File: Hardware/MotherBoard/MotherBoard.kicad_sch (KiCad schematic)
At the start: 24 parts, among them J1 POWER, J10 I/O_PWR, J13 USB_OTG, J2 I/O0, J5 I/O1, J6 EXTRN_CLCK, J9 Conn_02x02_Odd_Even, SW1 RESET_SW, SW2 ON_OFF, U1 AMS1117-5.0, X1 ACO-1MHz

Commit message: Fix
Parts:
- added F2: 500mA, Resistor_THT:R_Box_L8.4mm_W2.5mm_P5.08mm, symbol Device:Fuse_Small
- U1: footprint Package_TO_SOT_SMD:SOT-223-3_TabPin2 -> Package_TO_SOT_THT:TO-220-3_Horizontal_TabDown
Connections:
- net +5V: now also SW2.2 (B); no longer C2.1, FB2.2, U1.2 (VO)
- net at J13.1 (VBUS): now also F2.1; no longer FB2.1
- net at SW2.1 (A): now also C2.1, FB2.2, U1.2 (VO); no longer J1.1
- net at F1.1: now also J1.1; no longer SW2.2 (B)
- new net: F2.2, FB2.1
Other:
- sheet North Bridge ports: added DMARW, RW; removed none
- sheet South Bridge ports: added DMARW; removed none
- title: Retro 6502 Mother Board -> Miniish
- moved on the sheet: C1, C2, D1, F1, FB1, FB2, H1, H2, H3, H4, J1, J13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

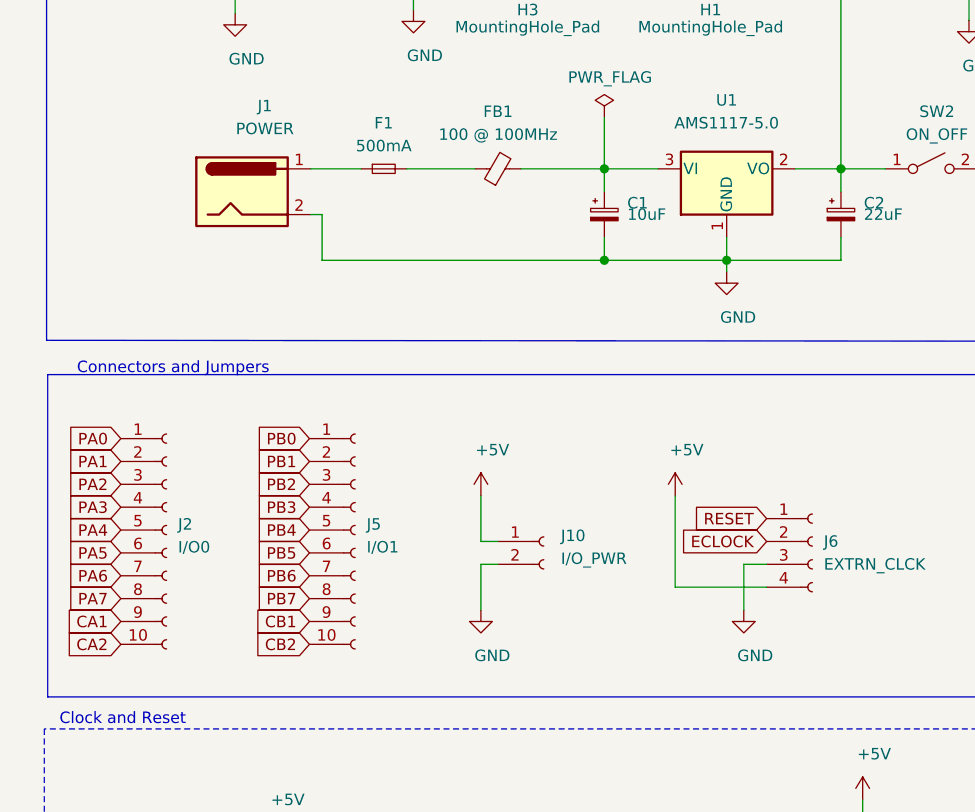
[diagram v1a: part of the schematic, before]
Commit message: Update to Kicad 6.0
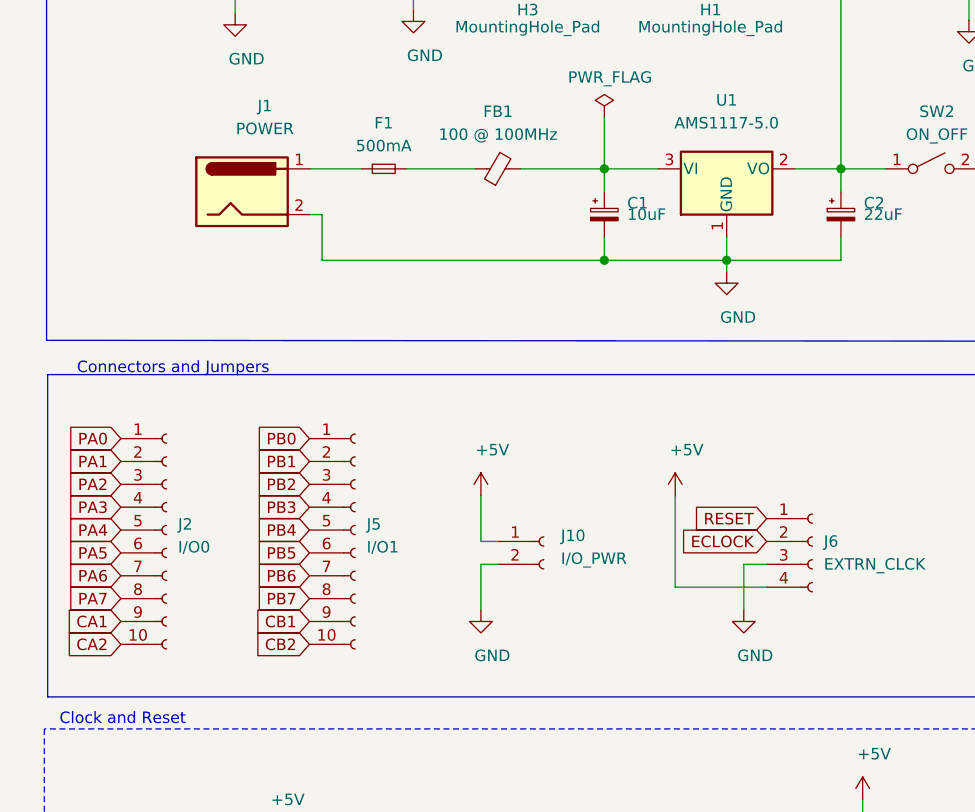
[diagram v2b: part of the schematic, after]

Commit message: New motherboard version
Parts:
- removed C8: 470nF, Capacitor_THT:C_Disc_D5.0mm_W2.5mm_P5.00mm, symbol Device:C_Small
- removed J10: I/O_PWR, Connector_PinSocket_2.54mm:PinSocket_1x02_P2.54mm_Vertical, symbol Connector:Conn_01x02_Female
- removed J2: I/O0, Connector_PinSocket_2.54mm:PinSocket_1x10_P2.54mm_Vertical, symbol Connector:Conn_01x10_Female
- removed J5: I/O1, Connector_PinSocket_2.54mm:PinSocket_1x10_P2.54mm_Vertical, symbol Connector:Conn_01x10_Female
- removed R3: 10K, Resistor_THT:R_Axial_DIN0207_L6.3mm_D2.5mm_P10.16mm_Horizontal, symbol Device:R_Small
- removed SW1: RESET_SW, Button_Switch_THT:SW_Tactile_SPST_Angled_PTS645Vx83-2LFS, symbol Switch:SW_Push
- added C1: 10nF, Capacitor_THT:C_Disc_D5.0mm_W2.5mm_P2.50mm, symbol Device:C
- added J11: CLOCK_DIV, Button_Switch_THT:SW_DIP_SPSTx05_Slide_6.7x14.26mm_W7.62mm_P2.54mm_LowProfile, symbol Switch:SW_DIP_x05
- added U1: 74HC590A, Package_DIP:DIP-16_W7.62mm, symbol 74xx:74HC590A
- C2: renamed from C1; symbol Device:CP_Small -> Device:C_Polarized_Small
- C3: renamed from C2; symbol Device:CP_Small -> Device:C_Polarized_Small
- FB1: renamed from FB2; symbol Device:Ferrite_Bead_Small -> Device:FerriteBead_Small
- FB2: renamed from FB1; symbol Device:Ferrite_Bead_Small -> Device:FerriteBead_Small
- J3: renamed from J9; value Conn_02x02_Odd_Even -> CLOCK_SEL
- J4: renamed from J6; symbol Connector:Conn_01x04_Female -> Connector:Conn_01x04_Socket
- U2: renamed from U1; symbol Regulator_Linear:AMS1117-5.0 -> Regulator_Linear:AZ1117-5.0
- X1: value ACO-1MHz -> ACO-16MHz
- renumbered F2 to F1, F1 to F2, H4 to H1, H3 to H2, H2 to H3, H1 to H4, J13 to J1, J1 to J2, R4 to R1
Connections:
- net +5V: now also C1.1, U1.10 (~{MRC}), U1.16 (VCC)
- net GND: now also C1.2, U1.12 (~{CE}), U1.14 (~{OE}), U1.8 (GND)
- net at J3.1 (Pin_1): now also J11.10, J11.6, J11.7, J11.8, J11.9; no longer X1.8 (OUT)
- new net 16MHz: J11.1, U1.11 (CPC), U1.13 (CPR), X1.8 (OUT)
- new net 1MHz: J11.5, U1.3 (Q3)
- new net 2MHz: J11.4, U1.2 (Q2)
- new net 4MHz: J11.3, U1.1 (Q1)
- new net 8MHz: J11.2, U1.15 (Q0)
- no-connect marks 3 -> 8
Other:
- removed sheet Main 
- added sheet GPIO (gpio.kicad_sch)
- added sheet Ports (ports.kicad_sch)
- sheet North Bridge: file /home/romuald/Projects/Miniish/Hardware/MotherBoard/NorthBridge.kicad_sch -> NorthBridge.kicad_sch
- sheet North Bridge ports: added NMIB, RESET; removed DMARW, IOCSB, IRQ0B, IRQ1B, PORT1B, PORT2B, ROMCSB
- sheet South Bridge: file /home/romuald/Projects/Miniish/Hardware/MotherBoard/SouthBridge.kicad_sch -> SouthBridge.kicad_sch
- sheet South Bridge ports: added CIA1CSB, CIA2CSB, IRQ1B, IRQ2B, IRQ3B, IRQ4B, IRQ5B, IRQ6B, IRQB, PORT1CSB, PORT2CSB, PORT3CSB, RAMCSB, ROMCSB, USRCSB; removed DMARW, NMIB, PORT1B, PORT2B, RESET, RW
- note added: "Clock"
- note removed: "Clock and Reset"
- note removed: "Connectors and Jumpers"
- moved on the sheet: H1, H2, H3, H4, J2, J3, J4, X1

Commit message: Finalize 1.3
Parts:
- J11: value CLOCK_DIV -> CLOCK_SPD
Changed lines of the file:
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@@
   (title_block
     (title "Miniish")
-    (date "2020-10-10")
+    (date "2023-05-19")
     (rev "v1.3")
     (company "Romuald Rousseau")
@@
       (effects (font (size 1.27 1.27)))
     )
-    (property "Value" "CLOCK_DIV" (at 102.87 95.25 0)
-      (effects (font (size 1.27 1.27)))
-    )
+    (property "Value" "CLOCK_SPD" (at 102.87 95.25 0)
+      (effects (font (size 1.27 1.27)))
+    )

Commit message: Version 1.3
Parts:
- added C1: 100nF, Capacitor_THT:C_Disc_D5.0mm_W2.5mm_P2.50mm, symbol Device:C
- C1: value 10nF -> 100nF
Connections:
- net GND: now also C1.2
- net RESET: now also C1.1
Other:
- moved on the sheet: J4
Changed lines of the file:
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@@
     (stroke (width 0) (type default))
   )
-  (wire (pts (xy 116.84 128.27) (xy 114.3 128.27))
+  (wire (pts (xy 119.38 129.54) (xy 116.84 129.54))
     (stroke (width 0) (type solid))
   )
@@
     (stroke (width 0) (type solid))
   )
-  (wire (pts (xy 114.3 128.27) (xy 114.3 133.35))
+  (wire (pts (xy 99.06 124.46) (xy 99.06 125.73))
+    (stroke (width 0) (type default))
+  )
+  (wire (pts (xy 116.84 129.54) (xy 116.84 134.62))
     (stroke (width 0) (type solid))
   )
@@
     (stroke (width 0) (type default))
   )
+  (wire (pts (xy 99.06 133.35) (xy 99.06 134.62))
+    (stroke (width 0) (type default))
+  )
   (wire (pts (xy 193.04 140.97) (xy 177.8 140.97))
     (stroke (width 0) (type default))
@@
     (stroke (width 0) (type default))
   )
-  (wire (pts (xy 106.68 120.65) (xy 106.68 130.81))
+  (wire (pts (xy 109.22 121.92) (xy 109.22 132.08))
     (stroke (width 0) (type solid))
   )
@@
     (stroke (width 0) (type solid))
   )
-  (wire (pts (xy 106.68 130.81) (xy 116.84 130.81))
+  (wire (pts (xy 109.22 132.08) (xy 119.38 132.08))
     (stroke (width 0) (type solid))
   )
@@
     (stroke (width 0) (type dash))
   )
+  (wire (pts (xy 119.38 124.46) (xy 99.06 124.46))
+    (stroke (width 0) (type default))
+  )
   (wire (pts (xy 177.8 104.14) (xy 177.8 55.88))
     (stroke (width 0) (type default))
@@
     (effects (font (size 1.27 1.27)) (justify left bottom))
   )
-  (global_label "ECLOCK" (shape input) (at 116.84 125.73 180)
+  (global_label "ECLOCK" (shape input) (at 119.38 127 180)
     (effects (font (size 1.27 1.27)) (justify right))
-    (property "Intersheetrefs" "${INTERSHEET_REFS}" (at 15.875 20.32 0)
-      (effects (font (size 1.27 1.27)) hide)
-    )
-  )
-  (global_label "RESET" (shape input) (at 116.84 123.19 180)
+    (property "Intersheetrefs" "${INTERSHEET_REFS}" (at 18.415 21.59 0)
+      (effects (font (size 1.27 1.27)) hide)
+    )
+  )
+  (global_label "RESET" (shape input) (at 99.06 124.46 180)
     (effects (font (size 1.27 1.27)) (justify right))
-    (property "Intersheetrefs" "${INTERSHEET_REFS}" (at 15.875 20.32 0)
+    (property "Intersheetrefs" "${INTERSHEET_REFS}" (at -1.905 21.59 0)
       (effects (font (size 1.27 1.27)) hide)
     )
@@
     )
   )
-  (symbol (lib_id "Connector:Conn_01x04_Socket") (at 121.92 125.73 0) (unit 1)
-    (in_bom yes) (on_board yes) (dnp no)
-    (property "Reference" "J4" (at 123.19 125.73 0)
+  (symbol (lib_id "Connector:Conn_01x04_Socket") (at 124.46 127 0) (unit 1)
+    (in_bom yes) (on_board yes) (dnp no)
+    (property "Reference" "J4" (at 125.73 127 0)
       (effects (font (size 1.27 1.27)) (justify left))
     )
-    (property "Value" "EXTRN_CLCK" (at 123.19 128.27 0)
+    (property "Value" "EXTRN_CLCK" (at 125.73 129.54 0)
       (effects (font (size 1.27 1.27)) (justify left))
     )
-    (property "Footprint" "Connector_PinHeader_2.54mm:PinHeader_1x04_P2.54mm_Vertical" (at 121.92 125.73 0)
-      (effects (font (size 1.27 1.27)) hide)
-    )
-    (property "Datasheet" "~" (at 121.92 125.73 0)
+    (property "Footprint" "Connector_PinHeader_2.54mm:PinHeader_1x04_P2.54mm_Vertical" (at 124.46 127 0)
+      (effects (font (size 1.27 1.27)) hide)
+    )
+    (property "Datasheet" "~" (at 124.46 127 0)
       (effects (font (size 1.27 1.27)) hide)
     )
@@
     )
   )
+  (symbol (lib_id "Device:C") (at 99.06 129.54 0) (unit 1)
+    (in_bom yes) (on_board yes) (dnp no)
+    (property "Reference" "C1" (at 102.108 127.254 0)
+      (effects (font (size 1.27 1.27)) (justify left))
+    )
+    (property "Value" "100nF" (at 102.108 129.794 0)
+      (effects (font (size 1.27 1.27)) (justify left))
+    )
+    (property "Footprint" "Capacitor_THT:C_Disc_D5.0mm_W2.5mm_P2.50mm" (at 100.0252 133.35 0)
+      (effects (font (size 1.27 1.27)) hide)
+    )
+    (property "Datasheet" "~" (at 99.06 129.54 0)
+      (effects (font (size 1.27 1.27)) hide)
+    )
+    (pin "1")
+    (pin "2")
+    (instances
+      (project "DaughterDevBoard"
+        (path "/635897ee-ca46-4488-aee3-87929b6a86bf"
+          (reference "C1") (unit 1)
+        )
+      )
+      (project "MotherBoard"
+        (path "/e63e39d7-6ac0-4ffd-8aa3-1841a4541b55"
+          (reference "C13") (unit 1)
+        )
+      )
+    )
+  )
   (symbol (lib_id "Device:C") (at 24.13 127 0) (unit 1)
     (in_bom yes) (on_board yes) (dnp no)
@@
       (effects (font (size 1.27 1.27)) (justify left))
     )
-    (property "Value" "10nF" (at 27.178 127.254 0)
+    (property "Value" "100nF" (at 27.178 127.254 0)
       (effects (font (size 1.27 1.27)) (justify left))
     )
@@
     )
   )
-  (symbol (lib_id "power:+5V") (at 106.68 120.65 0) (unit 1)
-    (in_bom yes) (on_board yes) (dnp no)
-    (property "Reference" "#PWR010" (at 106.68 124.46 0)
-      (effects (font (size 1.27 1.27)) hide)
-    )
-    (property "Value" "+5V" (at 107.95 115.57 0)
-      (effects (font (size 1.27 1.27)))
-    )
-    (property "Footprint" "" (at 106.68 120.65 0)
-      (effects (font (size 1.27 1.27)) hide)
-    )
-    (property "Datasheet" "" (at 106.68 120.65 0)
+  (symbol (lib_id "power:+5V") (at 109.22 121.92 0) (unit 1)
+    (in_bom yes) (on_board yes) (dnp no)
+    (property "Reference" "#PWR010" (at 109.22 125.73 0)
+      (effects (font (size 1.27 1.27)) hide)
+    )
+    (property "Value" "+5V" (at 110.49 116.84 0)
+      (effects (font (size 1.27 1.27)))
+    )
+    (property "Footprint" "" (at 109.22 121.92 0)
+      (effects (font (size 1.27 1.27)) hide)
+    )
+    (property "Datasheet" "" (at 109.22 121.92 0)
       (effects (font (size 1.27 1.27)) hide)
     )
@@
     )
   )
+  (symbol (lib_id "power:GND") (at 99.06 134.62 0) (unit 1)
+    (in_bom yes) (on_board yes) (dnp no)
+    (property "Reference" "#PWR0116" (at 99.06 140.97 0)
+      (effects (font (size 1.27 1.27)) hide)
+    )
+    (property "Value" "GND" (at 100.33 139.7 0)
+      (effects (font (size 1.27 1.27)))
+    )
+    (property "Footprint" "" (at 99.06 134.62 0)
+      (effects (font (size 1.27 1.27)) hide)
+    )
+    (property "Datasheet" "" (at 99.06 134.62 0)
+      (effects (font (size 1.27 1.27)) hide)
+    )
+    (pin "1")
+    (instances
+      (project "DaughterDevBoard"
+        (path "/635897ee-ca46-4488-aee3-87929b6a86bf"
+          (reference "#PWR0116") (unit 1)
+        )
+      )
+      (project "MotherBoard"
+        (path "/e63e39d7-6ac0-4ffd-8aa3-1841a4541b55"
+          (reference "#PWR026") (unit 1)
+        )
+      )
+    )
+  )
   (symbol (lib_id "Mechanical:MountingHole_Pad") (at 90.17 39.37 0) (unit 1)
     (in_bom yes) (on_board yes) (dnp no)
@@
     )
   )
-  (symbol (lib_id "power:GND") (at 114.3 133.35 0) (unit 1)
-    (in_bom yes) (on_board yes) (dnp no)
-    (property "Reference" "#PWR011" (at 114.3 139.7 0)
-      (effects (font (size 1.27 1.27)) hide)
-    )
-    (property "Value" "GND" (at 115.57 138.43 0)
-      (effects (font (size 1.27 1.27)))
-    )
-    (property "Footprint" "" (at 114.3 133.35 0)
-      (effects (font (size 1.27 1.27)) hide)
-    )
-    (property "Datasheet" "" (at 114.3 133.35 0)
-      (effects (font (size 1.27 1.27)) hide)
-    )
+  (symbol (lib_id "power:GND") (at 116.84 134.62 0) (unit 1)
+    (in_bom yes) (on_board yes) (dnp no)
+    (property "Reference" "#PWR011" (at 116.84 140.97 0)
+      (effects (font (size 1.27 1.27)) hide)
+    )
+    (property "Value" "GND" (at 118.11 139.7 0)
+      (effects (font (size 1.27 1.27)))
+    )
+    (property "Footprint" "" (at 116.84 134.62 0)
+      (effects (font (size 1.27 1.27)) hide)
+    )
+    (property "Datasheet" "" (at 116.84 134.62 0)
+      (effects (font (size 1.27 1.27)) hide)
+    )

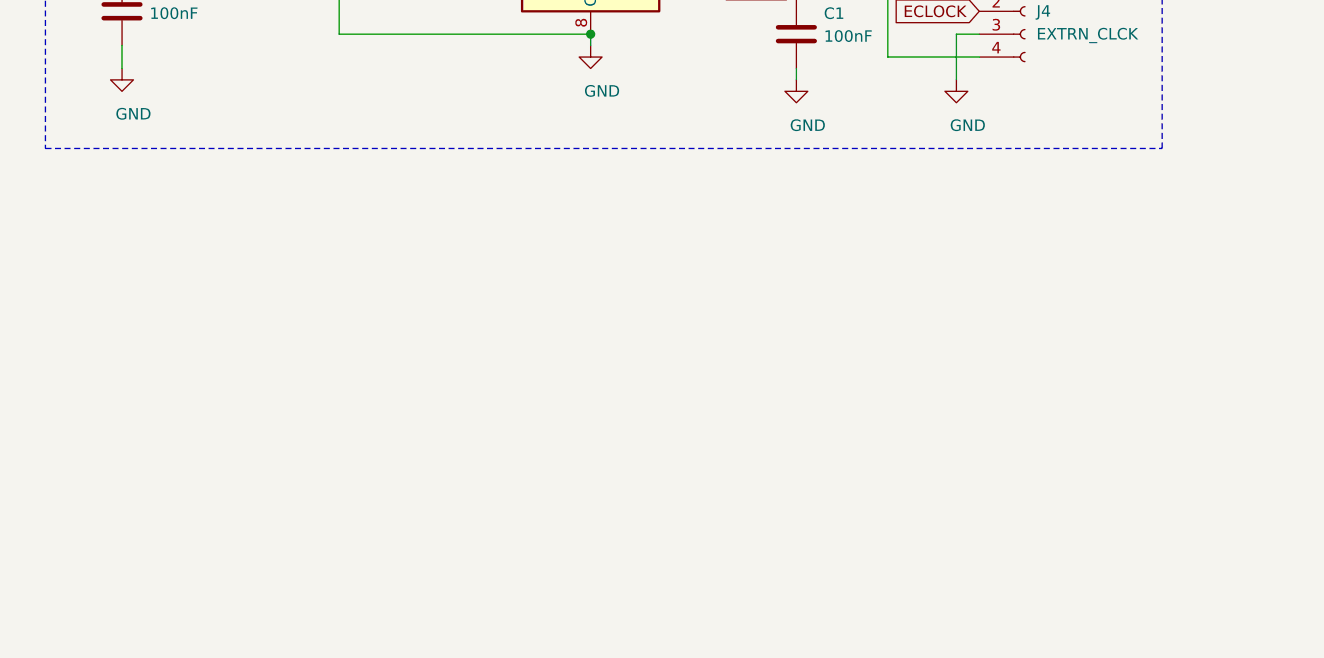
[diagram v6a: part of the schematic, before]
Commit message: Add SPI Board
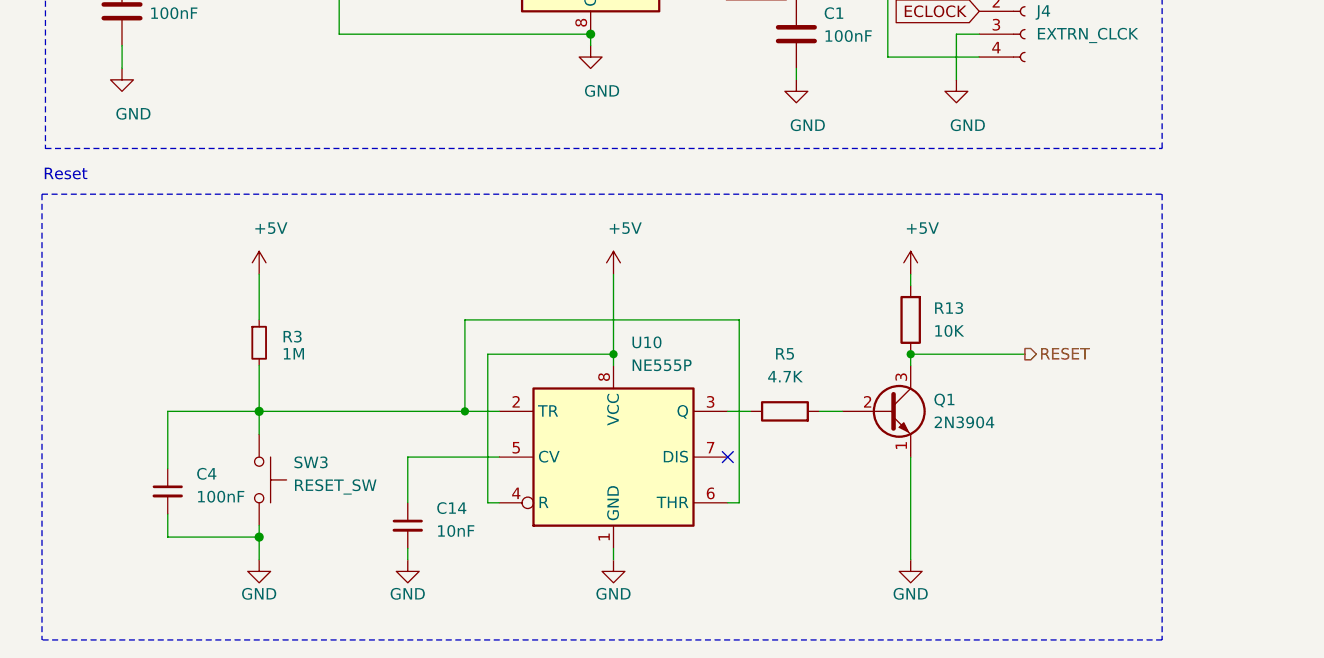
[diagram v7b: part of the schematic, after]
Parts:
- added C14: 10nF, Capacitor_THT:C_Disc_D5.0mm_W2.5mm_P5.00mm, symbol Device:C_Small
- added C4: 100nF, Capacitor_THT:C_Disc_D5.0mm_W2.5mm_P5.00mm, symbol Device:C_Small
- added Q1: 2N3904, Package_TO_SOT_THT:TO-92_Inline, symbol Transistor_BJT:2N3904
- added R13: 10K, Resistor_THT:R_Axial_DIN0207_L6.3mm_D2.5mm_P10.16mm_Horizontal, symbol Device:R
- added R3: 1M, Resistor_THT:R_Axial_DIN0207_L6.3mm_D2.5mm_P10.16mm_Horizontal, symbol Device:R_Small
- added R5: 4.7K, Resistor_THT:R_Axial_DIN0207_L6.3mm_D2.5mm_P10.16mm_Horizontal, symbol Device:R
- added SW3: RESET_SW, Button_Switch_THT:SW_Tactile_SPST_Angled_PTS645Vx83-2LFS, symbol Switch:SW_Push
- added U10: NE555P, Package_DIP:DIP-8_W7.62mm, symbol Timer:NE555P
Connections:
- net +5V: now also R13.2, R3.1, U10.4 (R), U10.8 (VCC)
- net GND: now also C14.2, C4.2, Q1.1 (E), SW3.2, U10.1 (GND)
- net RESET: now also Q1.3 (C), R13.1
- new net: C4.1, R3.2, SW3.1, U10.2 (TR), U10.6 (THR)
- new net: R5.1, U10.3 (Q)
- new net: Q1.2 (B), R5.2
- new net: C14.1, U10.5 (CV)
- no-connect marks 8 -> 9
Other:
- note added: "Reset"

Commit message: A lot of new hardware
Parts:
- removed C2: 10uF, Capacitor_THT:C_Radial_D5.0mm_H11.0mm_P2.00mm, symbol Device:C_Polarized_Small
- removed C3: 22uF, Capacitor_THT:C_Radial_D5.0mm_H11.0mm_P2.00mm, symbol Device:C_Polarized_Small
- removed D1: LED, LED_THT:LED_D5.0mm, symbol Device:LED
- removed F1, F2: 500mA, Resistor_THT:R_Box_L8.4mm_W2.5mm_P5.08mm, symbol Device:Fuse_Small
- removed FB1, FB2: 100 @ 100MHz, Inductor_THT:L_Axial_L9.5mm_D4.0mm_P12.70mm_Horizontal_Fastron_SMCC, symbol Device:FerriteBead_Small
- removed H1, H2, H3, H4: MountingHole_Pad, MountingHole:MountingHole_3.2mm_M3, symbol Mechanical:MountingHole_Pad
- removed J1: USB_OTG, Connector_USB:USB_B_OST_USB-B1HSxx_Horizontal, symbol Connector:USB_B
- removed J2: POWER, Connector_BarrelJack:BarrelJack_Horizontal, symbol Connector:Jack-DC
- removed R1: 220, Resistor_THT:R_Axial_DIN0207_L6.3mm_D2.5mm_P10.16mm_Horizontal, symbol Device:R
- removed U2: AMS1117-5.0, Package_TO_SOT_THT:TO-220-3_Horizontal_TabDown, symbol Regulator_Linear:AZ1117-5.0
- added D3: LED, LED_THT:LED_D5.0mm, symbol Device:LED
- added J25: ATX-24, Connector_Molex:Molex_Mini-Fit_Jr_5566-24A_2x12_P4.20mm_Vertical, symbol Connector:ATX-24
- added R14: 220, Resistor_THT:R_Axial_DIN0207_L6.3mm_D2.5mm_P10.16mm_Horizontal, symbol Device:R
- C14, C4: footprint Capacitor_THT:C_Disc_D5.0mm_W2.5mm_P5.00mm -> Capacitor_THT:C_Disc_D5.0mm_W2.5mm_P2.50mm
- SW3: value RESET_SW -> RESET
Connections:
- net +5V: now also J25.21 (+5V), J25.22 (+5V), J25.23 (+5V), J25.4 (+5V), J25.6 (+5V); no longer R3.1, SW2.2 (B)
- net GND: now also SW2.1 (A), J25.15 (GND), J25.17 (GND), J25.18 (GND), J25.19 (GND), J25.24 (GND), J25.3 (GND), J25.5 (GND), J25.7 (GND), R14.2
- new net: J25.1 (+3.3V), J25.12 (+3.3V), J25.13 (+3.3V), J25.2 (+3.3V)
- new net: J25.10 (+12V), J25.11 (+12V)
- new net: J25.16 (PS_ON#), SW2.2 (B)
- new net: D3.1 (K), R14.1
- new net PWR_OK: D3.2 (A), J25.8 (PWR_OK), R3.1
- no-connect marks 9 -> 10
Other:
- moved on the sheet: C1, C14, R13, R5, SW2
